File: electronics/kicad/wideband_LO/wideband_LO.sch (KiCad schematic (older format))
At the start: 56 parts, among them J1 CONN_06SMD, Q1 2N7002, Q2 BSS84, Q3 BSS84, U1 BFP620, U2 INA194

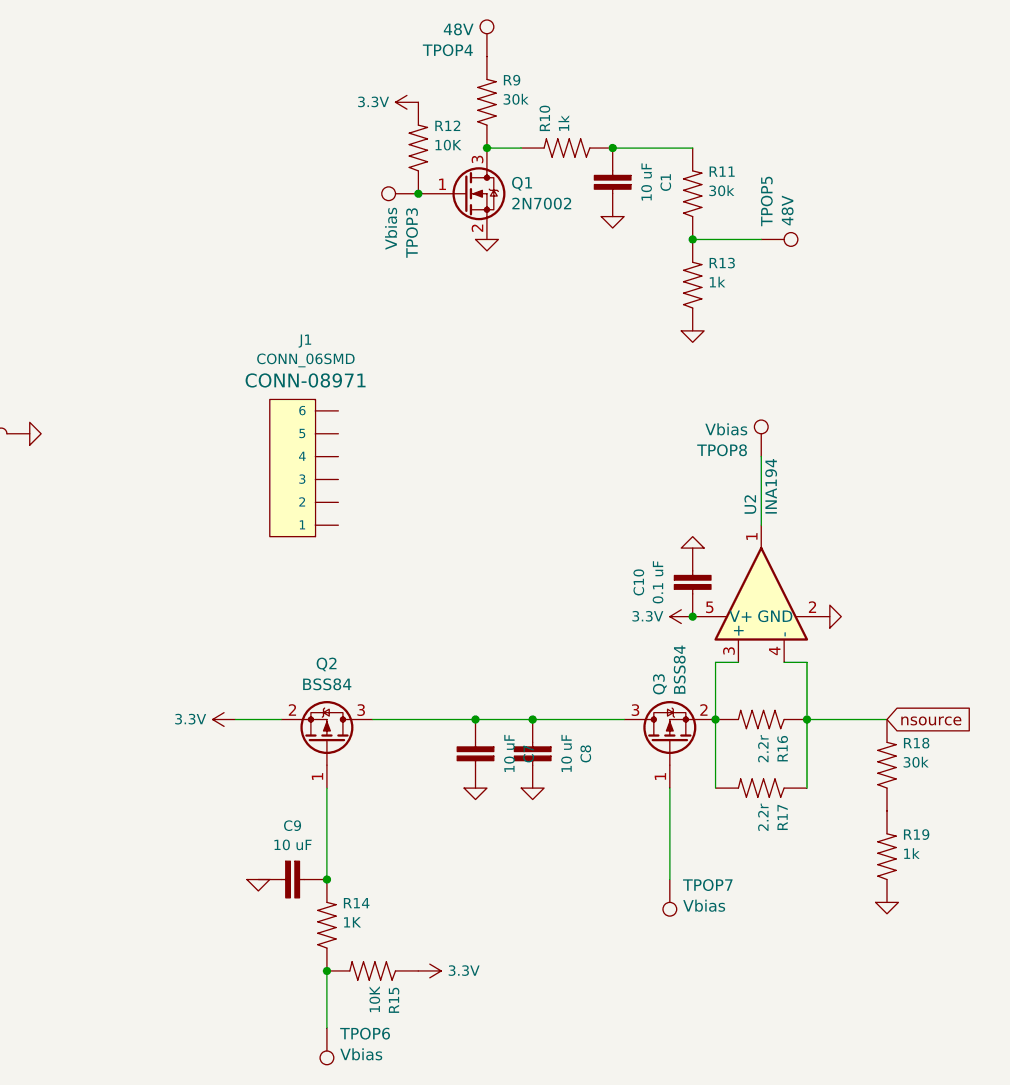
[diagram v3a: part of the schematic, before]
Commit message: Replaced decoupling caps
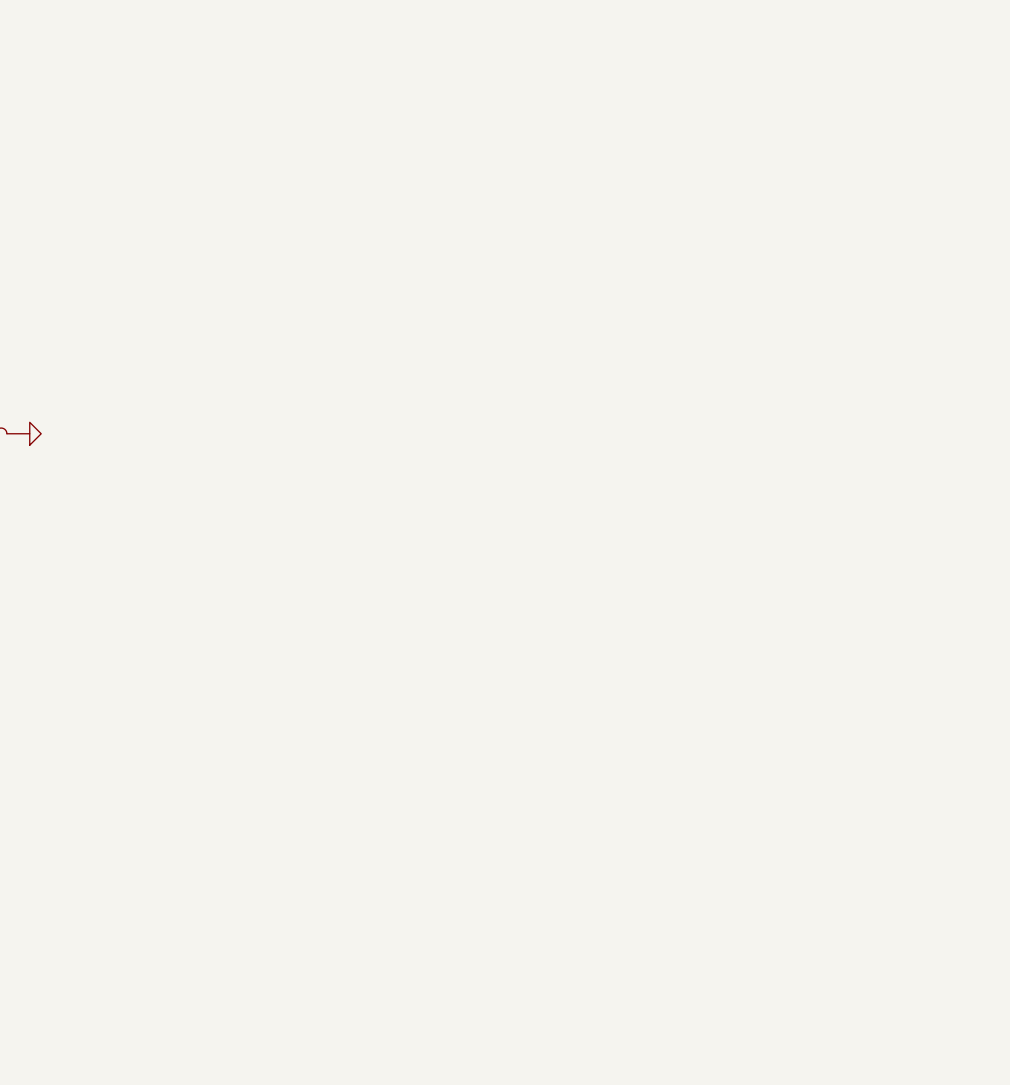
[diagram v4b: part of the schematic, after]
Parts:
- removed C1, C7, C8, C9: 10 uF, 0603, symbol SparkFun-Capacitors:4.7UF0603
- removed C10: 0.1 uF, 0603, symbol SparkFun-Capacitors:4.7UF0603
- removed J1: CONN_06SMD, 1X06-SMD_RA_MALE, symbol SparkFun-Connectors:CONN_06SMD
- removed Q1: 2N7002, Package_TO_SOT_SMD:SOT-23, symbol Transistor_FET:BSS138
- removed Q2, Q3: BSS84, Package_TO_SOT_SMD:SOT-23, symbol Transistor_FET:BSS84
- removed R10: 1k, Resistor_SMD:R_0402_1005Metric, symbol SparkFun-Resistors:RESISTOR0402
- removed R11, R18: 30k, Resistor_SMD:R_0603_1608Metric, symbol SparkFun-Resistors:RESISTOR0402
- removed R12, R15: 10K, Resistor_SMD:R_0402_1005Metric, symbol SparkFun-Resistors:RESISTOR0402
- removed R13, R19: 1k, Resistor_SMD:R_0603_1608Metric, symbol SparkFun-Resistors:RESISTOR0402
- removed R14: 1K, Resistor_SMD:R_0402_1005Metric, symbol SparkFun-Resistors:RESISTOR0402
- removed R16, R17: 2.2r, Resistor_SMD:R_0805_2012Metric, symbol SparkFun-Resistors:RESISTOR0402
- removed R9: 30k, Resistor_SMD:R_0603_1608Metric, symbol SparkFun-Resistors:0.05OHM-0603-1_5W-1%
- removed TPOP3, TPOP6, TPOP7, TPOP8: Vbias, TestPoint:TestPoint_Pad_1.5x1.5mm, symbol Connector:Test_Point
- removed TPOP4, TPOP5: 48V, TestPoint:TestPoint_Pad_1.5x1.5mm, symbol Connector:Test_Point
- removed U2: INA194, Package_TO_SOT_SMD:SOT-23-5, symbol Amplifier_Current:INA194
